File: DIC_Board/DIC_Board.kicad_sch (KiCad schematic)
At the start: 0 parts

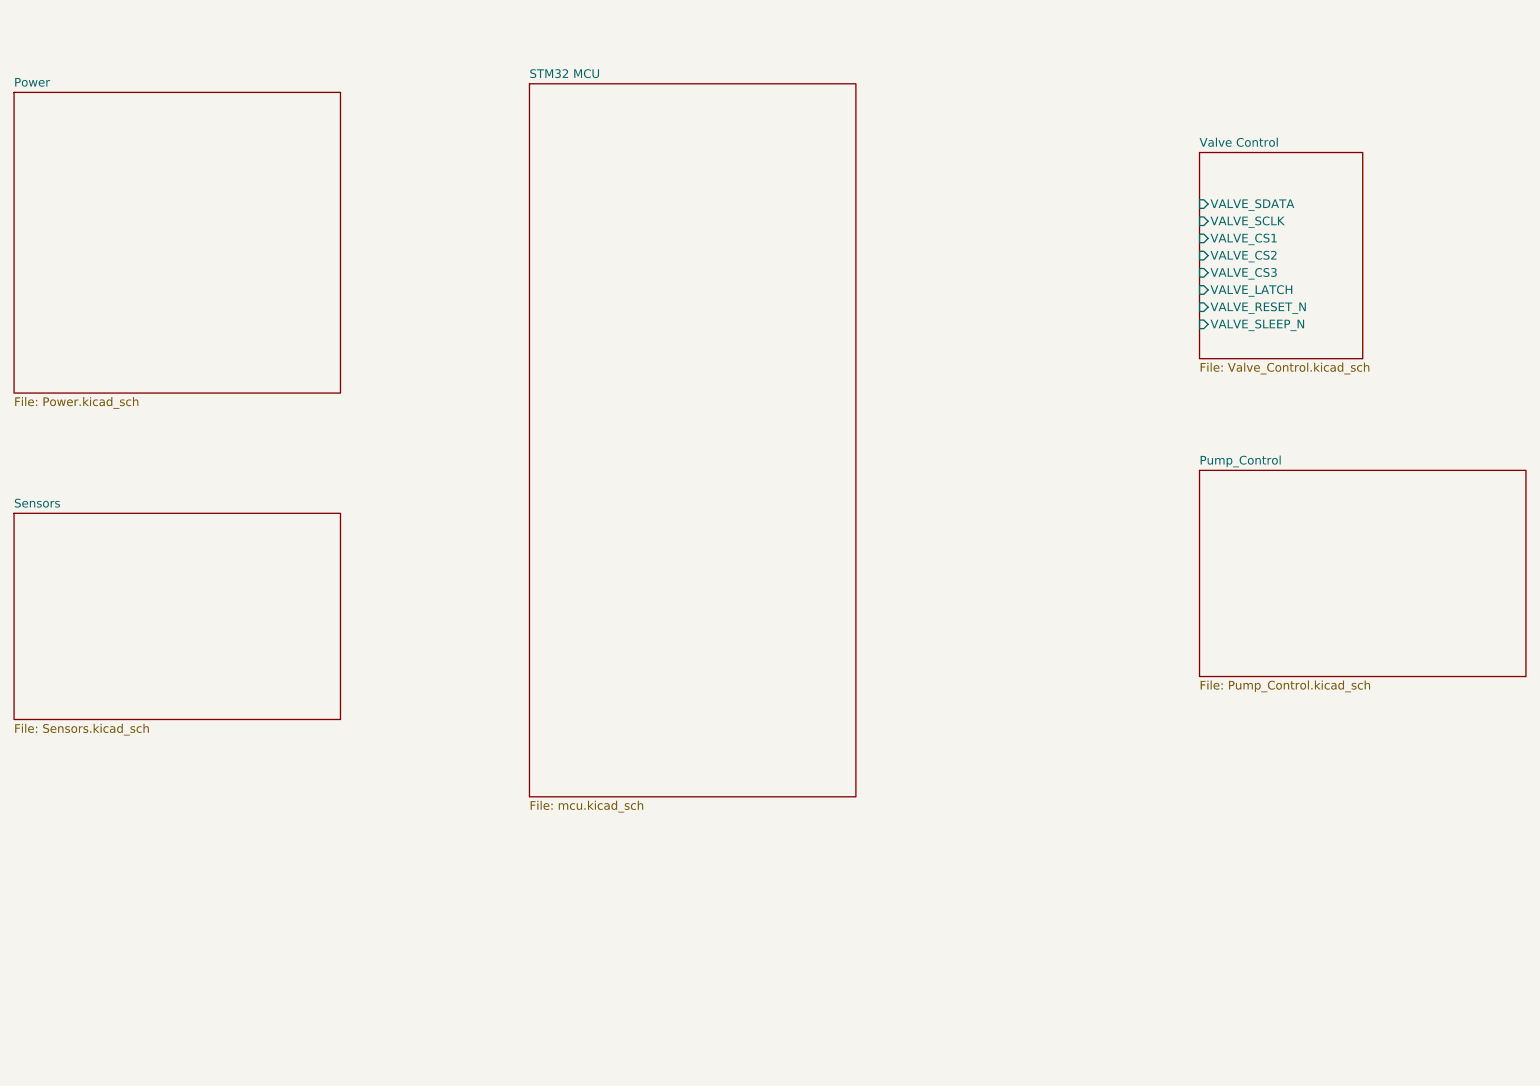
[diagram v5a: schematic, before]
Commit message: Separated the power sheets, did the sensor sheets.
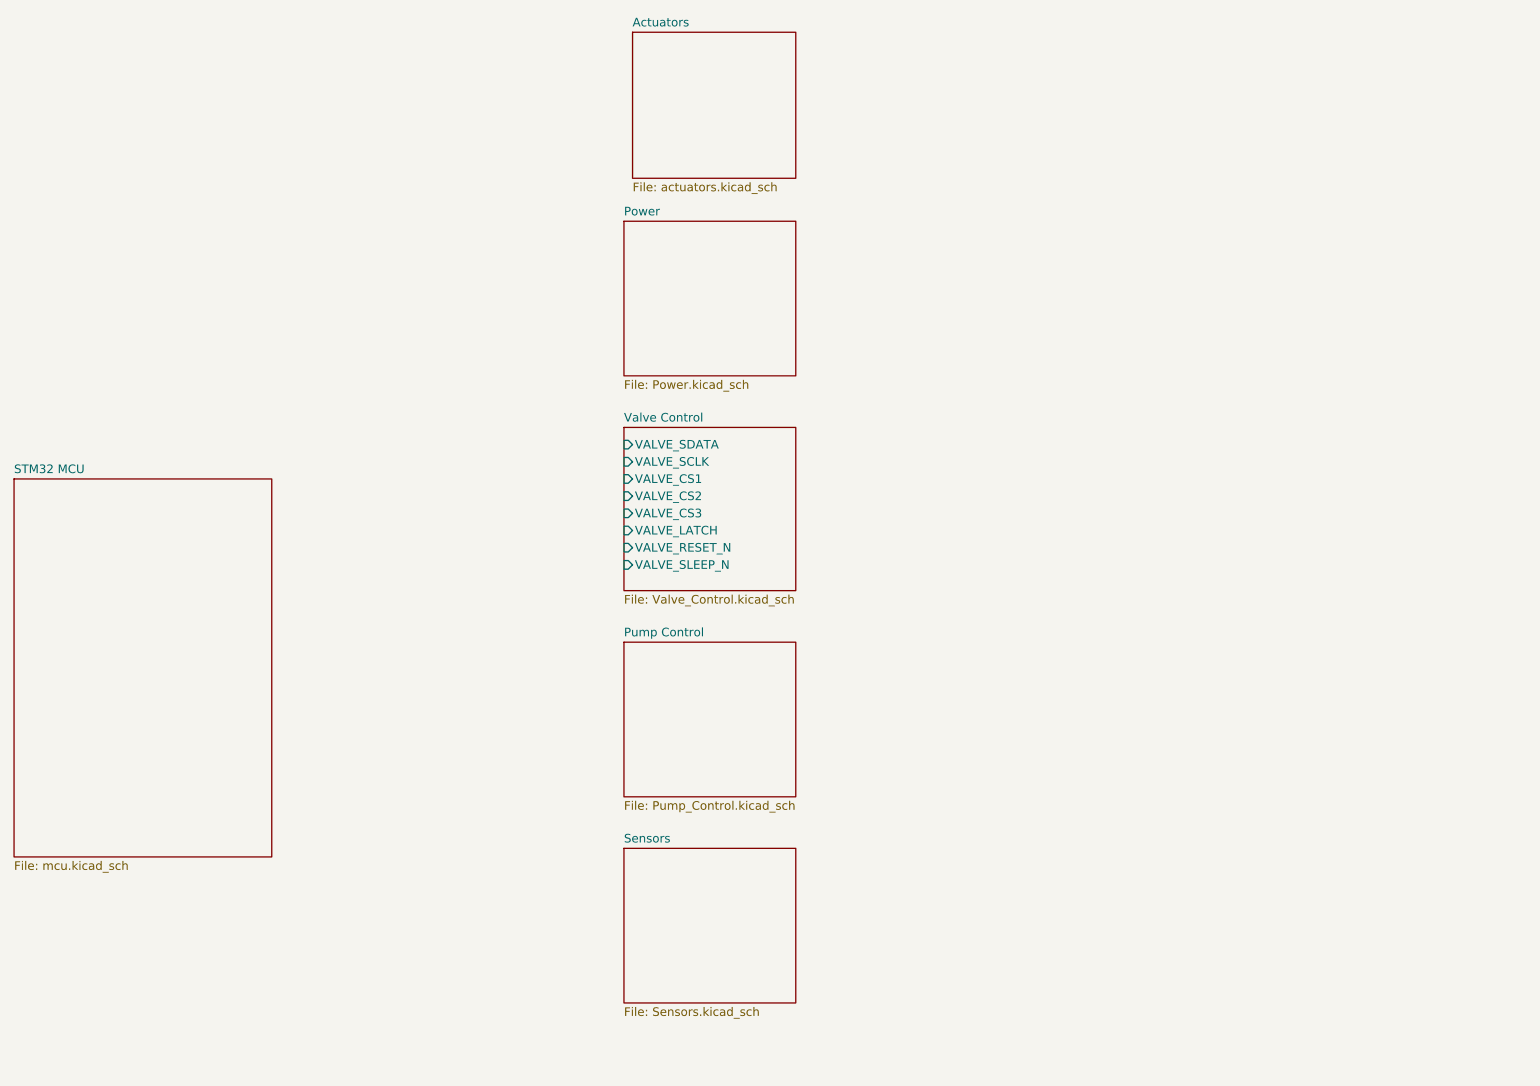
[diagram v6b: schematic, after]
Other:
- sheet Pump_Control renamed Pump Control
- added sheet Actuators (actuators.kicad_sch)
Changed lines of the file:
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@@
 	(paper "A4")
 	(sheet
-		(at 25.4 88.9)
-		(size 48.26 30.48)
+		(at 115.57 138.43)
+		(size 25.4 22.86)
 		(exclude_from_sim no)
 		(in_bom yes)
@@
 		)
 		(property "Sheetname" "Sensors"
-			(at 25.4 88.1884 0)
+			(at 115.57 137.7184 0)
 			(show_name no)
 			(do_not_autoplace no)
@@
 		)
 		(property "Sheetfile" "Sensors.kicad_sch"
-			(at 25.4 120.0146 0)
+			(at 115.57 161.8746 0)
 			(show_name no)
 			(do_not_autoplace no)
@@
 	)
 	(sheet
-		(at 200.66 35.56)
-		(size 24.13 30.48)
+		(at 116.84 17.78)
+		(size 24.13 21.59)
+		(exclude_from_sim no)
+		(in_bom yes)
+		(on_board yes)
+		(dnp no)
+		(fields_autoplaced yes)
+		(stroke
+			(width 0.1524)
+			(type solid)
+		)
+		(fill
+			(color 0 0 0 0)
+		)
+		(property "Sheetname" "Actuators"
+			(at 116.84 17.0684 0)
+			(show_name no)
+			(do_not_autoplace no)
+			(effects
+				(font
+					(size 1.27 1.27)
+				)
+				(justify left bottom)
+			)
+		)
+		(property "Sheetfile" "actuators.kicad_sch"
+			(at 116.84 39.9546 0)
+			(show_name no)
+			(do_not_autoplace no)
+			(effects
+				(font
+					(size 1.27 1.27)
+				)
+				(justify left top)
+			)
+		)
+		(instances
+			(project "DIC_Board"
+				(path "/bb0ef0df-c181-443a-843c-695cd2e0efee"
+					(page "22")
+				)
+			)
+		)
+	)
+	(sheet
+		(at 115.57 76.2)
+		(size 25.4 24.13)
 		(exclude_from_sim no)
 		(in_bom yes)
@@
 		)
 		(property "Sheetname" "Valve Control"
-			(at 200.66 34.8484 0)
+			(at 115.57 75.4884 0)
 			(show_name no)
 			(do_not_autoplace no)
@@
 		)
 		(property "Sheetfile" "Valve_Control.kicad_sch"
-			(at 200.66 66.6246 0)
+			(at 115.57 100.9146 0)
 			(show_name no)
 			(do_not_autoplace no)
@@
 		)
 		(pin "VALVE_SDATA" input
-			(at 200.66 43.18 180)
+			(at 115.57 78.74 180)
 			(effects
 				(font
@@
 		)
 		(pin "VALVE_SCLK" input
-			(at 200.66 45.72 180)
+			(at 115.57 81.28 180)
 			(effects
 				(font
@@
 		)
 		(pin "VALVE_CS1" input
-			(at 200.66 48.26 180)
+			(at 115.57 83.82 180)
 			(effects
 				(font
@@
 		)
 		(pin "VALVE_CS2" input
-			(at 200.66 50.8 180)
+			(at 115.57 86.36 180)
 			(effects
 				(font
@@
 		)
 		(pin "VALVE_CS3" input
-			(at 200.66 53.34 180)
+			(at 115.57 88.9 180)
 			(effects
 				(font
@@
 		)
 		(pin "VALVE_LATCH" input
-			(at 200.66 55.88 180)
+			(at 115.57 91.44 180)
 			(effects
 				(font
@@
 		)
 		(pin "VALVE_RESET_N" input
-			(at 200.66 58.42 180)
+			(at 115.57 93.98 180)
 			(effects
 				(font
@@
 		)
 		(pin "VALVE_SLEEP_N" input
-			(at 200.66 60.96 180)
+			(at 115.57 96.52 180)
 			(effects
 				(font
@@
 	)
 	(sheet
-		(at 25.4 26.67)
-		(size 48.26 44.45)
+		(at 115.57 45.72)
+		(size 25.4 22.86)
 		(exclude_from_sim no)
 		(in_bom yes)
@@
 		)
 		(property "Sheetname" "Power"
-			(at 25.4 25.9584 0)
+			(at 115.57 45.0084 0)
 			(show_name no)
 			(do_not_autoplace no)
@@
 		)
 		(property "Sheetfile" "Power.kicad_sch"
-			(at 25.4 71.7046 0)
+			(at 115.57 69.1646 0)
 			(show_name no)
 			(do_not_autoplace no)
@@
 	)
 	(sheet
-		(at 200.66 82.55)
-		(size 48.26 30.48)
-		(exclude_from_sim no)
-		(in_bom yes)
-		(on_board yes)
-		(dnp no)
-		(fields_autoplaced yes)
-		(stroke
-			(width 0.1524)
-			(type solid)
-		)
-		(fill
-			(color 0 0 0 0)
-		)
-		(property "Sheetname" "Pump_Control"
-			(at 200.66 81.8384 0)
+		(at 115.57 107.95)
+		(size 25.4 22.86)
+		(exclude_from_sim no)
+		(in_bom yes)
+		(on_board yes)
+		(dnp no)
+		(fields_autoplaced yes)
+		(stroke
+			(width 0.1524)
+			(type solid)
+		)
+		(fill
+			(color 0 0 0 0)
+		)
+		(property "Sheetname" "Pump Control"
+			(at 115.57 107.2384 0)
 			(show_name no)
 			(do_not_autoplace no)
@@
 		)
 		(property "Sheetfile" "Pump_Control.kicad_sch"
-			(at 200.66 113.6146 0)
+			(at 115.57 131.3946 0)
 			(show_name no)
 			(do_not_autoplace no)
@@
 	)
 	(sheet
-		(at 101.6 25.4)
-		(size 48.26 105.41)
+		(at 25.4 83.82)
+		(size 38.1 55.88)
 		(exclude_from_sim no)
 		(in_bom yes)
@@
 		)
 		(property "Sheetname" "STM32 MCU"
-			(at 101.6 24.6884 0)
+			(at 25.4 83.1084 0)
 			(show_name no)
 			(do_not_autoplace no)
@@
 		)
 		(property "Sheetfile" "mcu.kicad_sch"
-			(at 101.6 131.3946 0)
-			(show_name no)
-			(do_not_autoplace no)
+			(at 25.4 140.2846 0)
+			(show_name no)
+			(do_not_autoplace no)

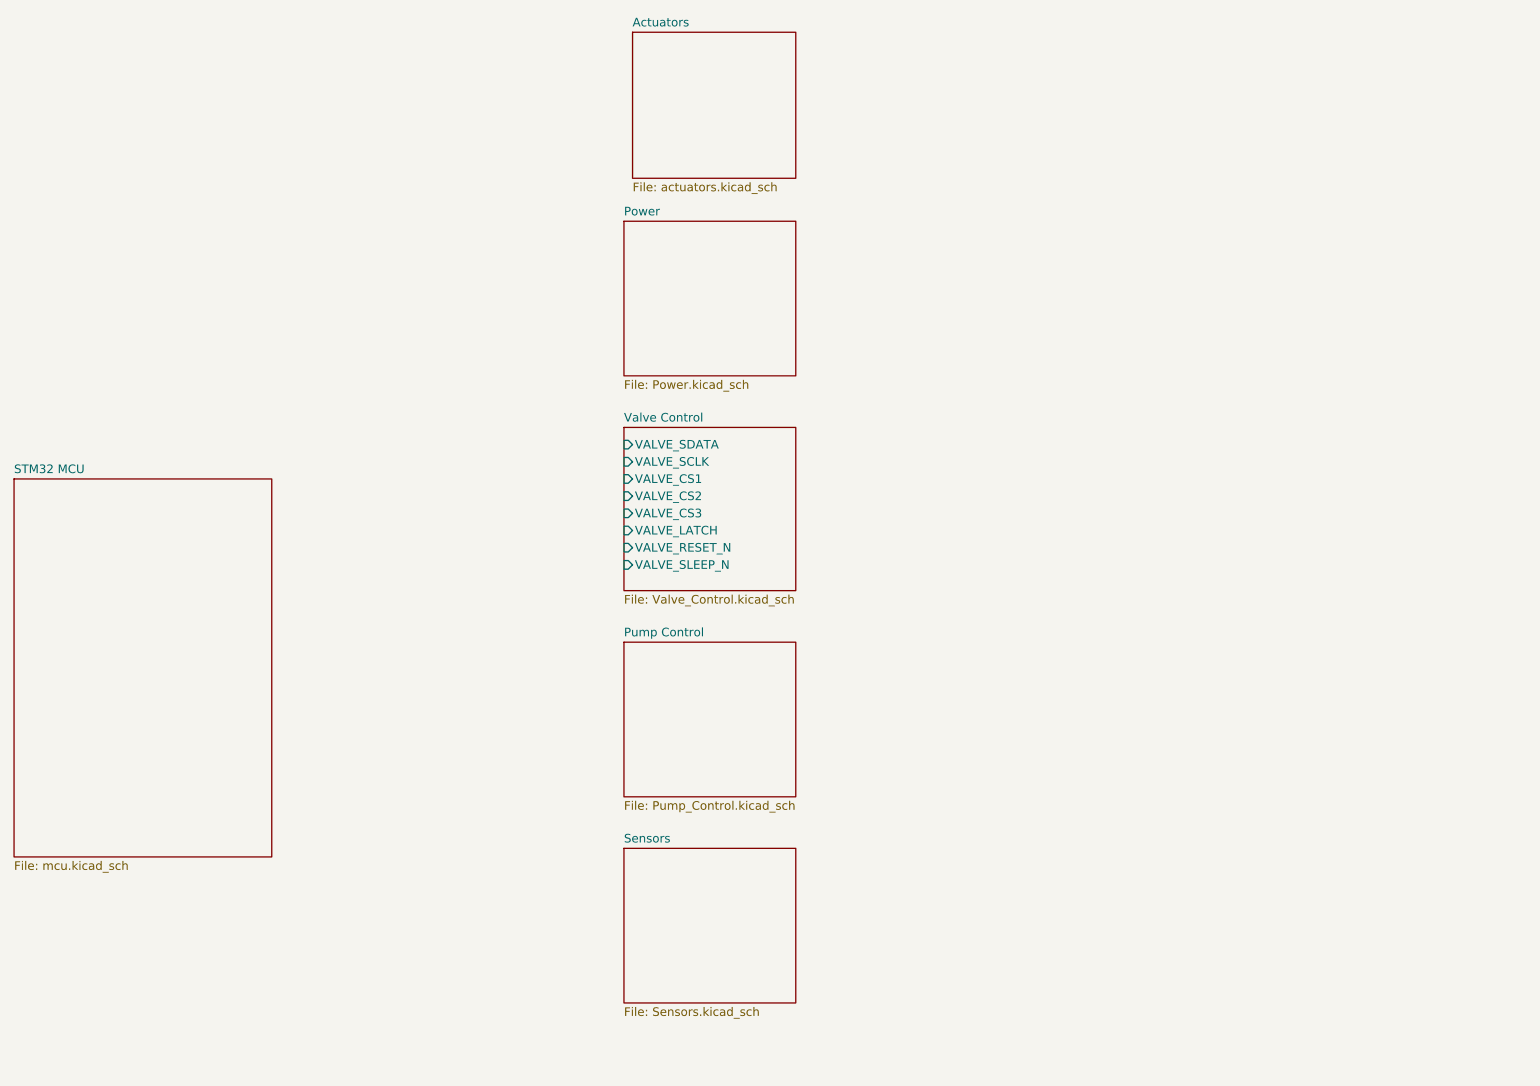
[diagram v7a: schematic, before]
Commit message: Synchronize schematic hierarchy and MCU pin map
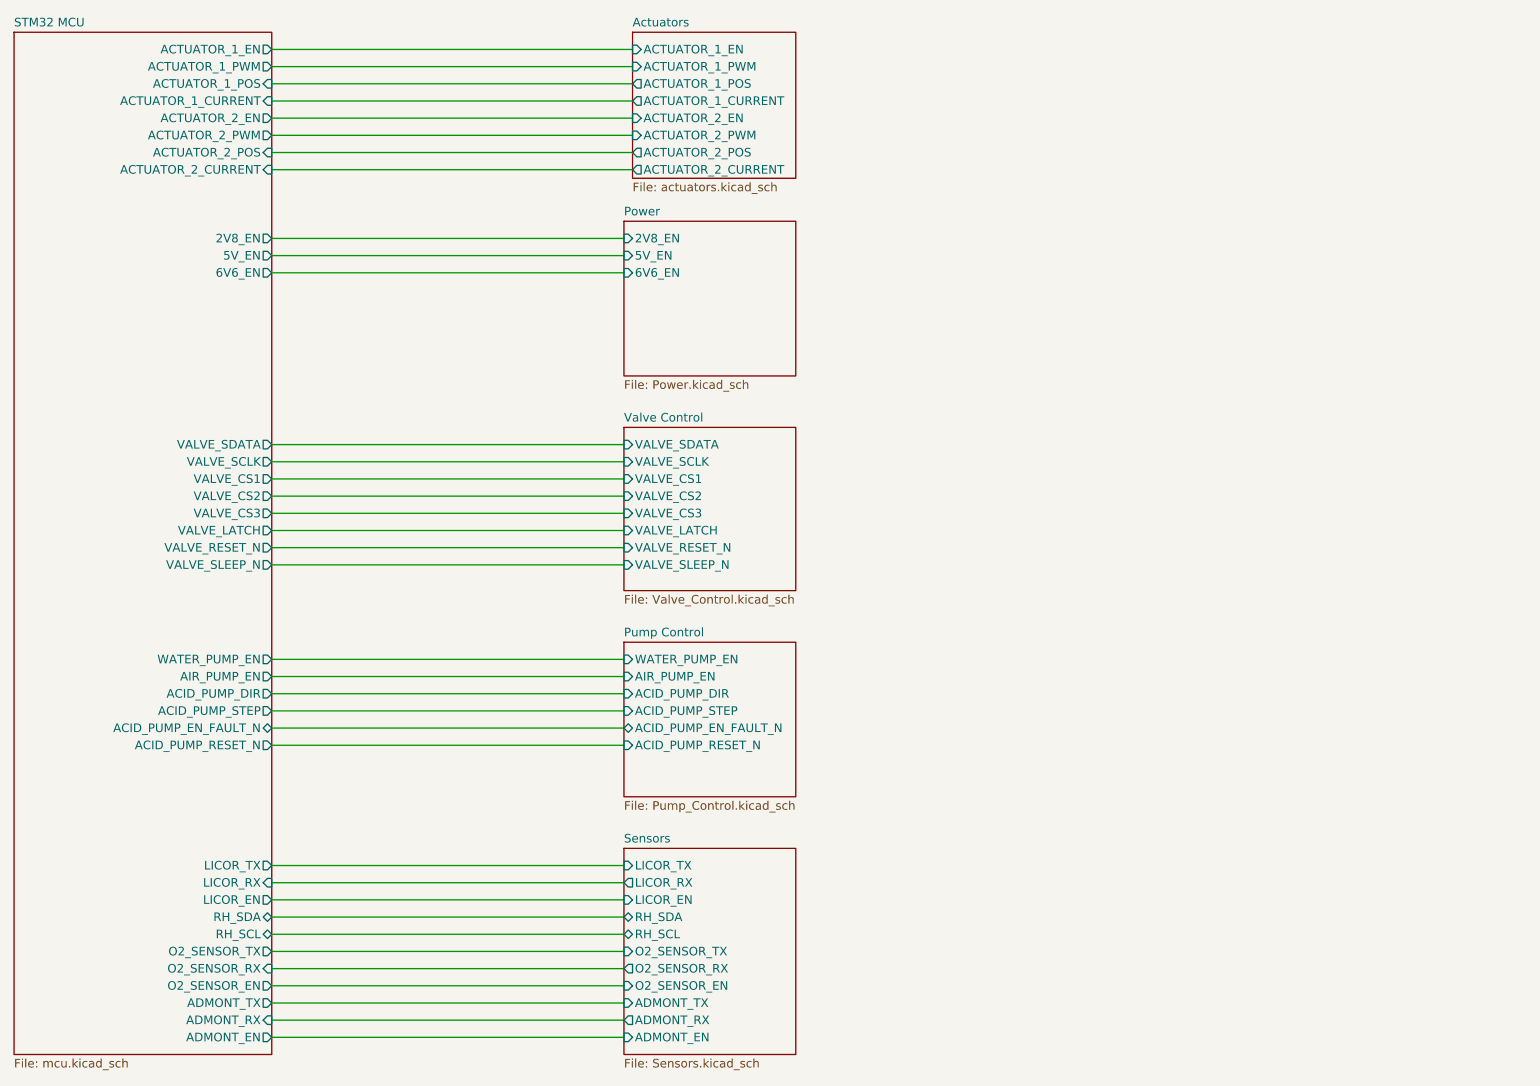
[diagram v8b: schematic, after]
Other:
- sheet Actuators ports: added ACTUATOR_1_CURRENT, ACTUATOR_1_EN, ACTUATOR_1_POS, ACTUATOR_1_PWM, ACTUATOR_2_CURRENT, ACTUATOR_2_EN, ACTUATOR_2_POS, ACTUATOR_2_PWM; removed none
- sheet Power ports: added 2V8_EN, 5V_EN, 6V6_EN; removed none
- sheet Pump Control ports: added ACID_PUMP_DIR, ACID_PUMP_EN_FAULT_N, ACID_PUMP_RESET_N, ACID_PUMP_STEP, AIR_PUMP_EN, WATER_PUMP_EN; removed none
- sheet STM32 MCU ports: added 2V8_EN, 5V_EN, 6V6_EN, ACID_PUMP_DIR, ACID_PUMP_EN_FAULT_N, ACID_PUMP_RESET_N, ACID_PUMP_STEP, ACTUATOR_1_CURRENT, ACTUATOR_1_EN, ACTUATOR_1_POS, ACTUATOR_1_PWM, ACTUATOR_2_CURRENT, ACTUATOR_2_EN, ACTUATOR_2_POS, ACTUATOR_2_PWM, ADMONT_EN, ADMONT_RX, ADMONT_TX, AIR_PUMP_EN, LICOR_EN, LICOR_RX, LICOR_TX, O2_SENSOR_EN, O2_SENSOR_RX, O2_SENSOR_TX, RH_SCL, RH_SDA, VALVE_CS1, VALVE_CS2, VALVE_CS3, VALVE_LATCH, VALVE_RESET_N, VALVE_SCLK, VALVE_SDATA, VALVE_SLEEP_N, WATER_PUMP_EN; removed none
- sheet Sensors ports: added ADMONT_EN, ADMONT_RX, ADMONT_TX, LICOR_EN, LICOR_RX, LICOR_TX, O2_SENSOR_EN, O2_SENSOR_RX, O2_SENSOR_TX, RH_SCL, RH_SDA; removed none
